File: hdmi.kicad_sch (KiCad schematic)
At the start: 41 parts, among them J7 685119136923, Q2 PJE138K, Q3 PJE138K, U12 NTS0102, U13 TPD4E05U06QDQARQ1, U14 TPD4E05U06QDQARQ1, U15 TPD4E05U06QDQARQ1

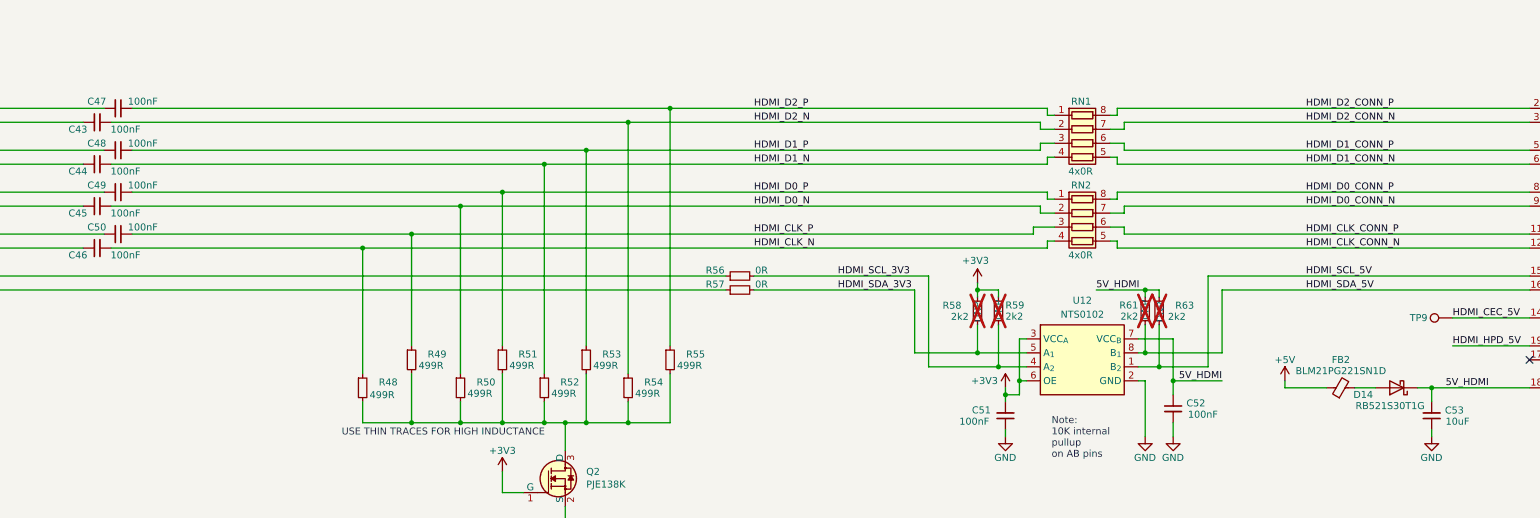
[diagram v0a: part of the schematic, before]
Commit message: Replace current monitor w/ INA226 (addr = 0x42)
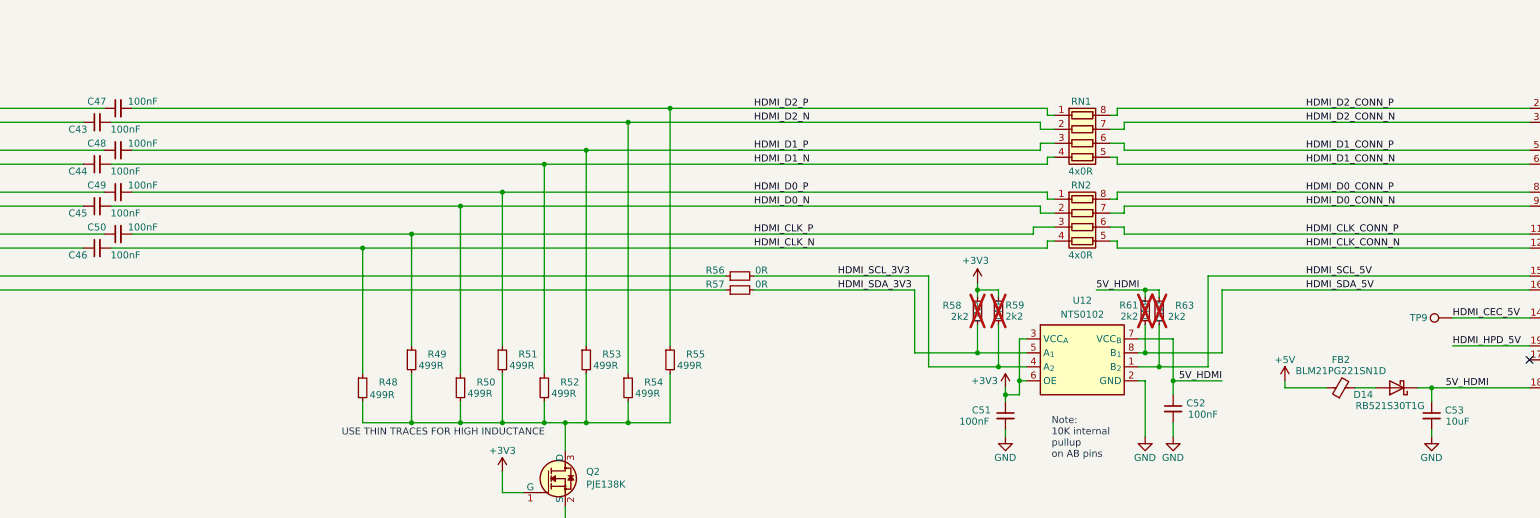
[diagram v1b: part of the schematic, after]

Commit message: Final cleanup, production files
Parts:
- removed Q2, Q3: PJE138K, Package_TO_SOT_SMD:SOT-523, symbol JetsonCarrier:PJE138K
- added Q2, Q3: 2N7002, Package_TO_SOT_SMD:SOT-23, symbol Transistor_FET:2N7002
- FB2: footprint Inductor_SMD:L_0603_1608Metric -> Inductor_SMD:L_0805_2012Metric
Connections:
- net +3V3: now also Q2.1 (G)
- net DP1_HPD: now also Q3.3 (D)
- net GND: now also Q2.2 (S), Q3.2 (S)
- net HDMI_HPD_5V_R: now also Q3.1 (G)
- net at R48.2, R49.2, R50.2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: now also Q2.3 (D)
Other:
- moved on the sheet: R62, R64

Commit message: Final BOM changes, gerbers
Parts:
- C43, C44, C45, C46, C47, C48, C49, C50: LCSC (none) -> C307331
- C51, C52: LCSC (none) -> C14663
- C53: LCSC (none) -> C96446
- D14: LCSC (none) -> C145179
- FB2: LCSC (none) -> C85840
- J7: LCSC (none) -> C2961651
- Q2, Q3: LCSC (none) -> C8545
- R48, R49, R50, R51, R52, R53, R54, R55: LCSC (none) -> C4125
- R56, R57: LCSC (none) -> C17168
- R58, R59, R61, R63: LCSC (none) -> C25879
- R60: LCSC (none) -> C25804
- R62, R64: LCSC (none) -> C25803
- RN1, RN2: LCSC (none) -> C2001
- U12: LCSC (none) -> C2687851
- U13, U14, U15: LCSC (none) -> C81353
